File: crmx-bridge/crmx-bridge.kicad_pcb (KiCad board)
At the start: 4 copper layers, 100.5 x 76.8 mm, 94 parts, among them IC101 ESP32-S3-WROOM-1U-N4R2, J101 AFC07-S16FCC-00, J102 NC3FAAH2, J103 USB_C_Receptacle_USB2.0_16P, J104 NC3MAAH, J105 Conn_01x02_Pin, J106 AFC07-S16FCC-00, J201 Conn_01x04_Pin, Q101 DMP4025SFGQ-13, Q102 AO3400A, U101 TIMOTWO, U102 AP63200WU, U103 ISO3088DW, U104 SRV05-4, U105 ISO3088DW, U106 TEA1-0505, U107 TEA1-0505, U201 PEC12R-4215F-S0024

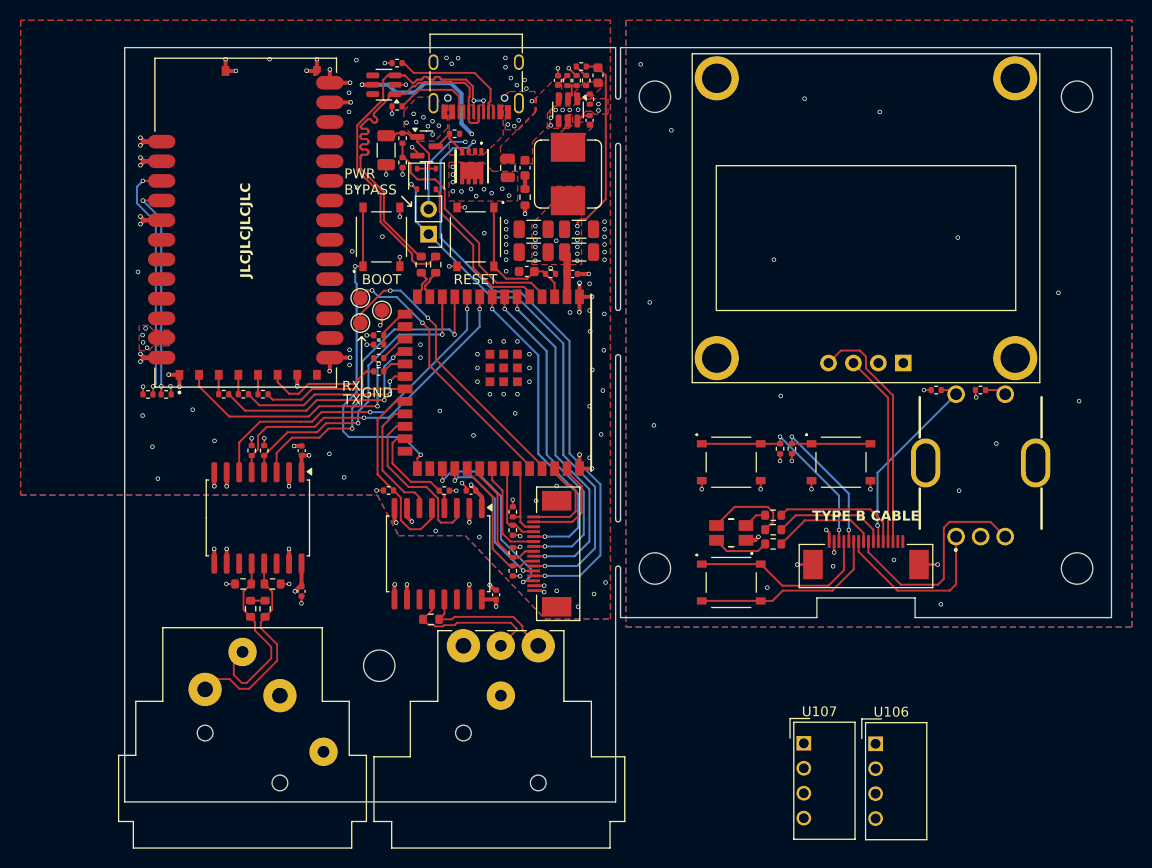
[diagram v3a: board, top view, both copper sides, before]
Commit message: smaller isolated supplies integrated, may re-arrange some more
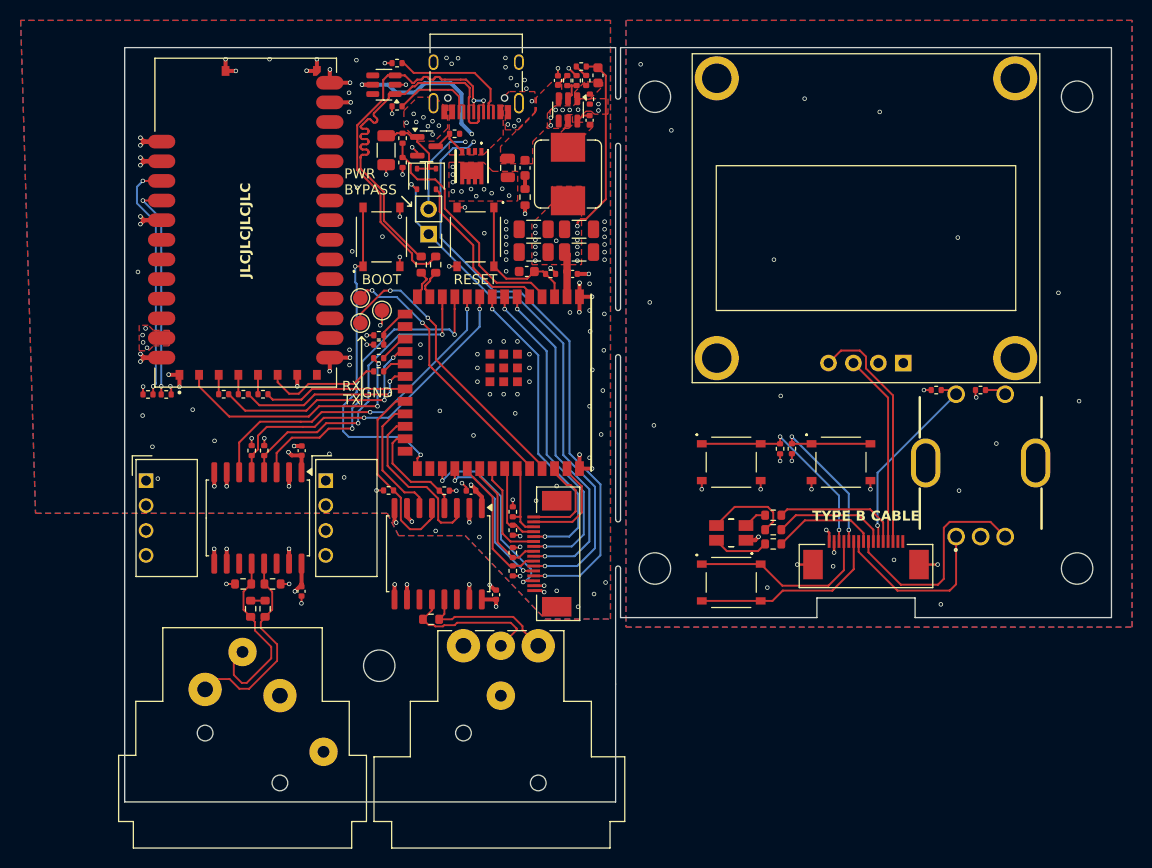
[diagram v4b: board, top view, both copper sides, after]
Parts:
- moved U107 72.1 mm to (119.5, 61.9)
- moved U106 62.1 mm to (137.8, 61.9)
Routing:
- net +3V3: track 37.7 -> 37.2 mm
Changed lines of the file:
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@@
 	(footprint "Converter_DCDC:Converter_DCDC_TRACO_TEA1-xxxx_THT"
 		(layer "F.Cu")
-		(at 186.4425 88.6075)
+		(at 119.45 61.85)
 		(descr "DCDC-Converter, TRACO, TEA1-xxxx, 1W, Rev. October 19. 2023 (Script generated with StandardBox.py) (https://www.tracopower.com/products/tea1.pdf)")
 		(tags "DCDC-Converter TRACO TEA1 THT SIP-4 1W")
@@
 			(at 1.6 -3.23 0)
 			(layer "F.SilkS")
+			(hide yes)
 			(effects
 				(font
@@
 	(footprint "Converter_DCDC:Converter_DCDC_TRACO_TEA1-xxxx_THT"
 		(layer "F.Cu")
-		(at 193.75 88.65)
+		(at 137.75 61.85)
 		(descr "DCDC-Converter, TRACO, TEA1-xxxx, 1W, Rev. October 19. 2023 (Script generated with StandardBox.py) (https://www.tracopower.com/products/tea1.pdf)")
 		(tags "DCDC-Converter TRACO TEA1 THT SIP-4 1W")
@@
 			(at 1.6 -3.23 0)
 			(layer "F.SilkS")
+			(hide yes)
 			(effects
 				(font
@@
 	)
 	(segment
+		(start 134.28 59.28)
+		(end 133.95 58.95)
+		(width 0.4064)
+		(layer "F.Cu")
+		(net 2)
+	)
+	(segment
+		(start 135.3 59.28)
+		(end 134.28 59.28)
+		(width 0.4064)
+		(layer "F.Cu")
+		(net 2)
+	)
+	(segment
 		(start 153.03 62.875)
 		(end 153.03 62.755)
@@
 	)
 	(segment
-		(start 135.285 59.295)
-		(end 135.3 59.28)
-		(width 0.4064)
-		(layer "F.Cu")
-		(net 2)
-	)
-	(segment
-		(start 136.045 59.28)
-		(end 136.05 59.275)
-		(width 0.4064)
-		(layer "F.Cu")
-		(net 2)
-	)
-	(segment
 		(start 156.8 71.55)
 		(end 157.525 71.55)
@@
 	)
 	(segment
-		(start 135.3 59.28)
-		(end 136.045 59.28)
-		(width 0.4064)
-		(layer "F.Cu")
-		(net 2)
-	)
-	(segment
 		(start 166.275 20.6)
 		(end 165.475 19.8)
@@
 	)
 	(via
-		(at 136.05 59.275)
-		(size 0.45)
-		(drill 0.3)
-		(layers "F.Cu" "B.Cu")
-		(net 2)
-	)
-	(via
 		(at 159.1 38.05)
 		(size 0.45)
@@
 	)
 	(via
+		(at 133.95 58.95)
+		(size 0.45)
+		(drill 0.3)
+		(layers "F.Cu" "B.Cu")
+		(net 2)
+	)
+	(via
 		(at 152.55 62.275)
 		(size 0.45)
@@
 	)
 	(segment
-		(start 136.05 59.275)
-		(end 136.05 60.525)
-		(width 0.4064)
-		(layer "In2.Cu")
-		(net 2)
-	)
-	(segment
 		(start 126.395 68.81)
 		(end 126.385 68.8)
@@
 		(polygon
 			(pts
-				(xy 143 63.325) (xy 145.175 67.45) (xy 151.961075 67.45) (xy 160.096321 75.95) (xy 166.75 75.95)
-				(xy 166.75 14.975) (xy 106.675 14.975) (xy 106.675 63.325)
+				(xy 144.017544 65.175) (xy 145.175 67.45) (xy 151.961075 67.45) (xy 160.096321 75.95) (xy 166.75 75.95)
+				(xy 166.75 14.975) (xy 106.675 14.975) (xy 108.19238 65.175)
 			)
 		)
@@
 		(polygon
 			(pts
-				(xy 166.797475 84.423806) (xy 151.904272 68.651888) (xy 144.364521 68.651888) (xy 142.5 64.925)
-				(xy 139.75 64.925) (xy 139.75 71.656336) (xy 141.752021 75.752797) (xy 141.752021 96.036888) (xy 166.777021 96.036888)
+				(xy 166.797475 84.423806) (xy 151.904272 68.651888) (xy 144.364521 68.651888) (xy 143.150376 66.225)
+				(xy 136.75 66.225) (xy 136.75 70.775621) (xy 141.752021 75.752797) (xy 141.752021 96.036888) (xy 166.777021 96.036888)
 			)
 		)
@@
 		(polygon
 			(pts
-				(xy 143 63.325) (xy 145.175 67.45) (xy 151.950717 67.45) (xy 160.090352 75.961826) (xy 166.75 75.966448)
-				(xy 166.75 16.875) (xy 115.075 16.875) (xy 115.075 63.325)
+				(xy 144.004824 65.15) (xy 145.175 67.45) (xy 151.950717 67.45) (xy 160.090352 75.961826) (xy 166.75 75.966448)
+				(xy 166.75 16.875) (xy 115.075 16.875) (xy 114.94856 65.15)
 			)
 		)
@@
 		(polygon
 			(pts
-				(xy 140.025 75.75) (xy 138.175 72) (xy 138.175 64.91) (xy 110.6 64.91) (xy 110.6 96.01) (xy 140.025 96.01)
+				(xy 140.025 75.75) (xy 135.75 71.639424) (xy 135.75 66.21) (xy 110.725 66.21) (xy 110.6 96.01) (xy 140.025 96.01)
 			)
 		)
@@
 		(polygon
 			(pts
-				(xy 166.795448 84.425033) (xy 151.901462 68.65) (xy 144.3625 68.65) (xy 142.5 64.925) (xy 139.75 64.925)
-				(xy 139.75 71.631725) (xy 141.75 75.72555) (xy 141.75 96.035) (xy 166.775 96.035)
+				(xy 166.795448 84.425033) (xy 151.901462 68.65) (xy 144.3625 68.65) (xy 143.15 66.225) (xy 136.8 66.225)
+				(xy 136.777251 70.802251) (xy 141.75 75.72555) (xy 141.75 96.035) (xy 166.775 96.035)
 			)
 		)
@@
 		(polygon
 			(pts
-				(xy 149.525 28.95) (xy 158.1 28.8) (xy 158.1 44.575) (xy 142.925 59.75) (xy 121.625 59.75) (xy 121.625 56.275)
-				(xy 124.35 53.55) (xy 136.825 53.55) (xy 149.525 40.85)
+				(xy 149.525 28.95) (xy 158.1 28.8) (xy 158.1 44.575) (xy 138.725 65.125) (xy 118.325 65.125) (xy 118.325 59.6)
+				(xy 134.55 59.6) (xy 149.525 44.625)
 			)
 		)
@@
 		(polygon
 			(pts
-				(xy 140.025 75.75) (xy 138.175 72) (xy 138.175 64.91) (xy 107.7 64.91) (xy 107.7 100.235) (xy 140.025 99.975)
+				(xy 140.025 75.75) (xy 135.75 71.644867) (xy 135.75 66.21) (xy 107.825 66.21) (xy 107.7 100.235)
+				(xy 140.025 99.975)
 			)
 		)
@@
 		(polygon
 			(pts
-				(xy 143 63.325) (xy 145.175 67.45) (xy 151.983187 67.45) (xy 160.100769 75.95) (xy 166.75 75.95)
-				(xy 166.75 14.975) (xy 108.675 14.975) (xy 108.675 63.325)
+				(xy 144.004824 65.15) (xy 145.175 67.45) (xy 151.983187 67.45) (xy 160.100769 75.95) (xy 166.75 75.95)
+				(xy 166.75 14.975) (xy 108.675 14.975) (xy 108.599169 65.15)
 			)
 		)

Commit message: Rev to v0.2
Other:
- board text added: "DMX IO Device HMI V0.2 Chris Markus, 2024"
- board text added: "DMX IO Device V0.2 Chris Markus, 2024"
- board text removed: "DMX IO Device HMI V0.1 Chris Markus, 2024"
- board text removed: "DMX IO Device V0.1 Chris Markus, 2024"
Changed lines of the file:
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@@
 		(layer "Edge.Cuts")
 	)
-	(gr_text "DMX IO Device HMI V0.1\nChris Markus, 2024"
+	(gr_text "DMX IO Device HMI V0.2\nChris Markus, 2024"
 		(at 192.775 37.8 0)
 		(layer "B.SilkS")
@@
 		)
 	)
-	(gr_text "DMX IO Device V0.1\nChris Markus, 2024"
+	(gr_text "DMX IO Device V0.2\nChris Markus, 2024"
 		(at 142.275 47.575 0)
 		(layer "B.SilkS")

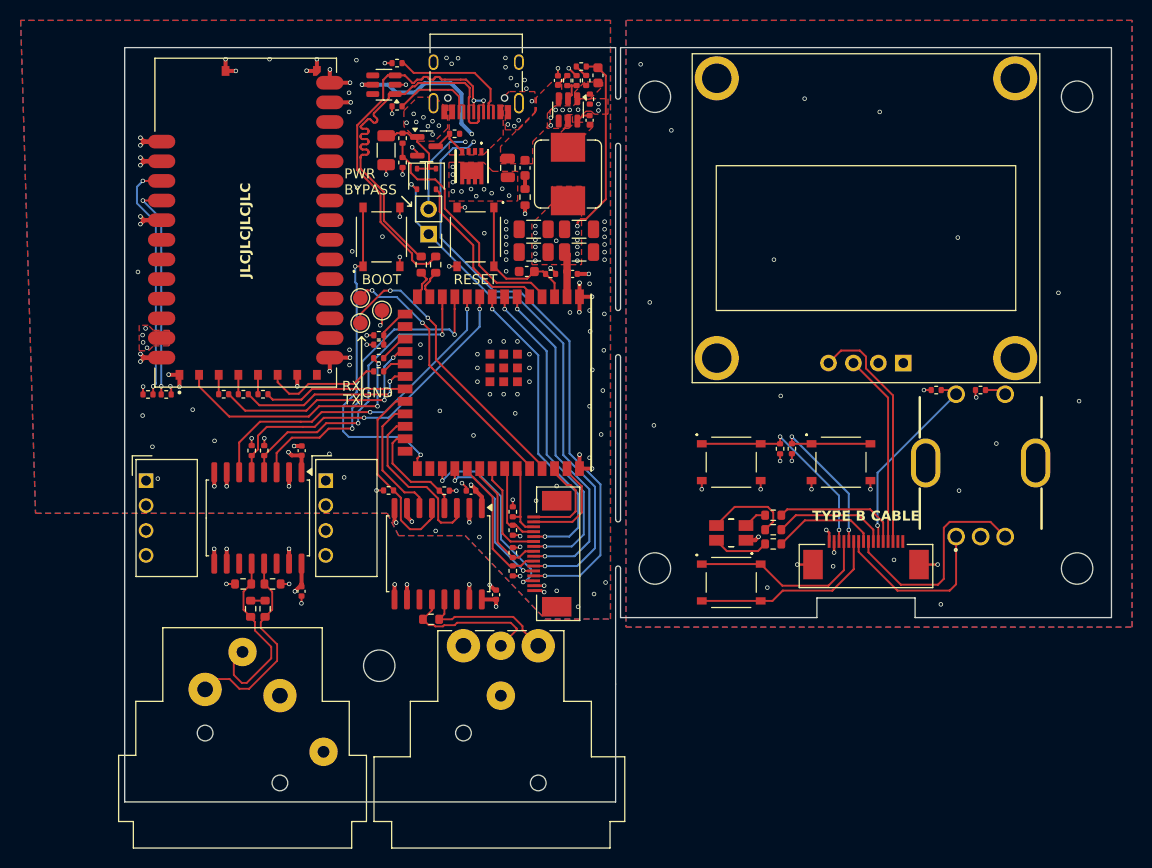
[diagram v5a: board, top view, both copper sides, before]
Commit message: Finished layout with smaller power converters
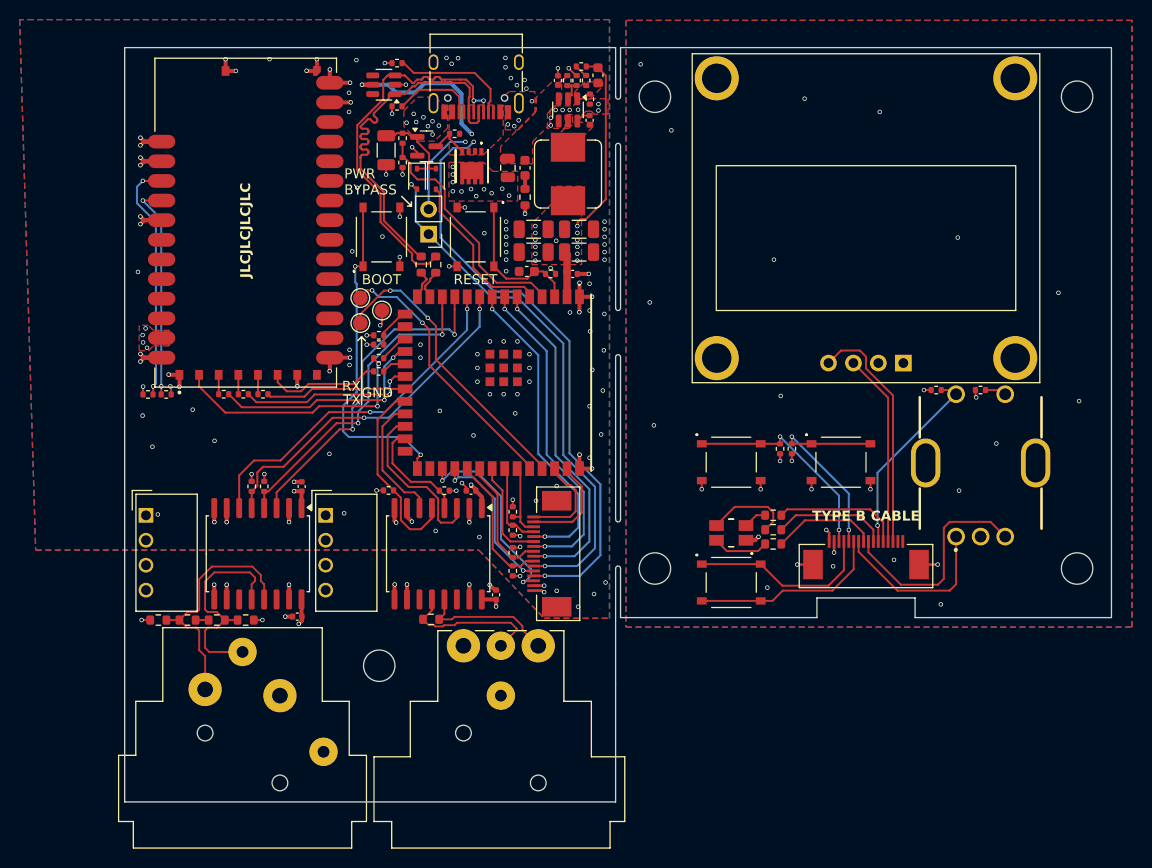
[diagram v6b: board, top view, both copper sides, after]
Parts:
- moved R105 12.2 mm to (120.7, 76.0), turned to 180 degrees
- moved R125 7.98 mm to (123.7, 76.0), turned to 180 degrees
- moved R104 3.68 mm to (129.6, 76.0), turned to 180 degrees
- moved C101 3.65 mm to (135.3, 62.5)
- moved R121 3.65 mm to (130.2, 62.4)
- moved R122 3.65 mm to (131.5, 62.4)
- moved U103 3.65 mm to (130.8, 69.3)
- moved R103 3.64 mm to (126.7, 76.0), turned to 180 degrees
- moved U106 3.53 mm to (137.7, 65.4)
- moved U107 3.53 mm to (119.4, 65.4)
- moved C102 2.61 mm to (134.8, 75.7), turned to 180 degrees
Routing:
- net /DMX_OUT_N: track 20.7 -> 25.4 mm
- net /DMX_OUT_P: track 19.0 -> 22.8 mm
- net /DMX_OUT_TX: track 34.4 -> 36.1 mm
- net /DMX_OUT_NRE: track 31.6 -> 33.1 mm
- net /DMX_OUT_DE: track 34.2 -> 35.7 mm
- net /DMX_OUT_RX: track 32.8 -> 34.2 mm
- net +3V3: track 37.2 -> 36.5 mm

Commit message: Split up PCBs into separate files, Ordered V0.3
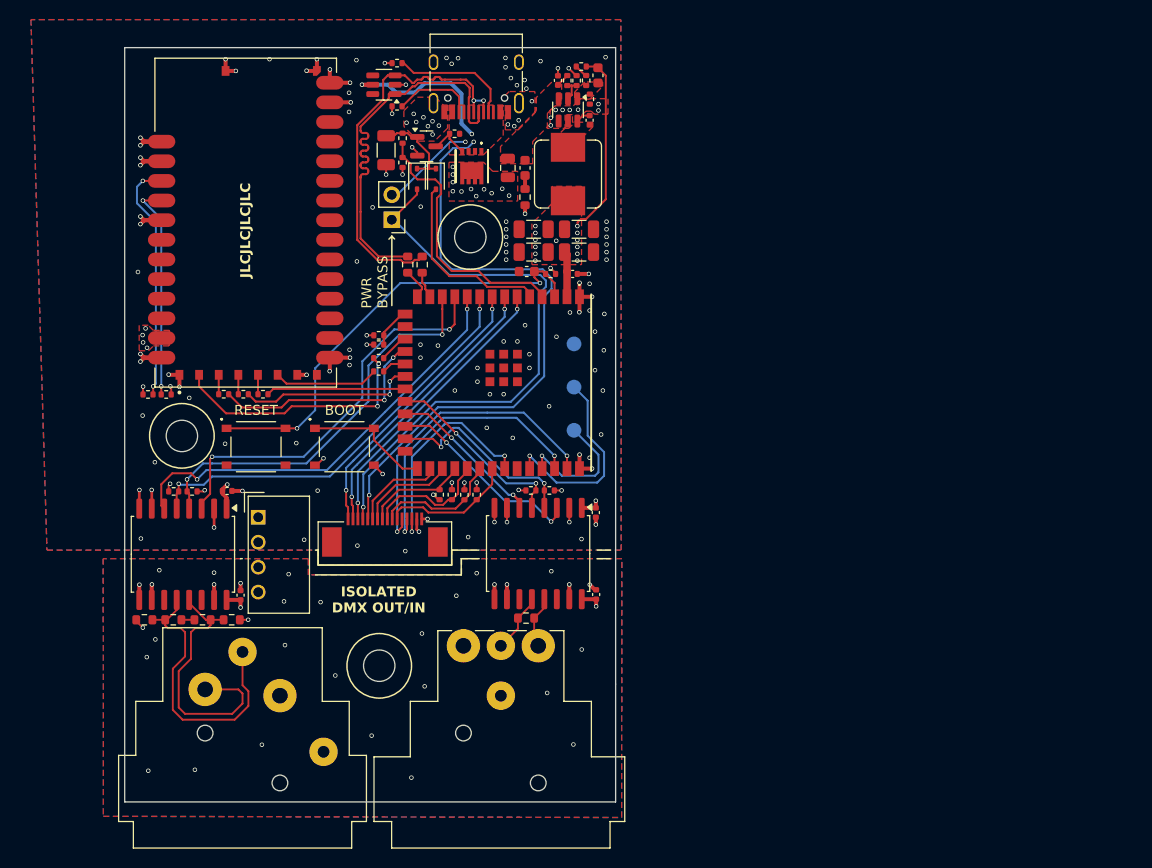
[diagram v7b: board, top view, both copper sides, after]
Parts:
- removed D201: ASMB-MTB0-0A3A2, ASMB-MTB0-0A3A2:ASMBMTB00A3A2
- removed H104, H105: MountingHole, MountingHole:MountingHole_3.2mm_M3
- removed J101: AFC07-S16FCC-00, AFC07-S16FCC-00:AFC07S16FCC00
- removed J201: Conn_01x04_Pin, Oled:OLED_1.3
- removed R205, R207, R208: 10k, Resistor_SMD:R_0402_1005Metric
- removed R206: 0R, Resistor_SMD:R_0402_1005Metric
- removed R209, R210, R211: 150, Resistor_SMD:R_0603_1608Metric
- removed S201, S202, S203: TS-1187A-B-A-B, LIB_TS-1187A-B-A-B:TS1187ABAB
- removed U107: TEA1-0505, Converter_DCDC:Converter_DCDC_TRACO_TEA1-xxxx_THT
- removed U201: PEC12R-4215F-S0024, PEC12R:PEC12R-4XXXF-SXXXX
- TP101, TP102, TP103: moved to B.Cu
- moved H103 97.5 mm to (123.1, 57.3)
- moved H102 70.4 mm to (152.5, 37.0)
- moved S101 30.9 mm to (130.7, 58.4), turned to 0 degrees
- moved TP102 24.4 mm to (163.0, 56.7), turned to 0 degrees
- moved TP101 23.6 mm to (163.0, 52.3), turned to 0 degrees
- moved S102 21.7 mm to (139.7, 58.4), turned to 0 degrees
- moved TP103 19.9 mm to (163.0, 47.9), turned to 180 degrees
- moved J106 17.5 mm to (143.8, 68.1), turned to 0 degrees
- moved R126 14.5 mm to (158.6, 62.9)
- moved C113 12.9 mm to (165.3, 65.1), turned to -90 degrees
- moved R113 10.8 mm to (149.3, 63.3)
- moved R127 10.7 mm to (160.5, 62.9)
- moved R104 10.3 mm to (119.3, 76.0), turned to 0 degrees
- moved C114 10.2 mm to (165.3, 73.5)
- moved U105 10.2 mm to (159.4, 69.3)
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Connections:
- C102 pad 1: /VCC_ISO_2 -> /VCC_ISO
- C102 pad 2: /GND_ISO_2 -> GNDS
- C114 pad 1: /VCC_ISO_1 -> /VCC_ISO
- C114 pad 2: /GND_ISO_1 -> GNDS
- IC101 pad 28: unconnected-(IC101-IO35-Pad28) -> /OK_BTN
- IC101 pad 29: /OK_BTN -> /BK_BTN
- IC101 pad 30: /BK_BTN -> /ENC1.A
- IC101 pad 31: /ENC1.A -> /ENC1.B
- IC101 pad 32: /ENC1.B -> /OLED_SCL
- IC101 pad 33: /ENC1.SW -> /OLED_SDA
- IC101 pad 34: /OLED_SCL -> /ENC1.SW
- IC101 pad 35: /OLED_SDA -> unconnected-(IC101-IO42-Pad35)
- J102 pad 1: /GND_ISO_2 -> GNDS
- J102 pad G: /GND_ISO_2 -> GNDS
- J104 pad 1: /GND_ISO_1 -> GNDS
- J104 pad G: /GND_ISO_1 -> GNDS
- J106 pad 1: GND -> /LED_R
- J106 pad 10: /LED_G -> /OLED_SCL
- J106 pad 11: /ENC1.SW -> /OLED_SDA
- J106 pad 12: /LED_R -> /IO1
- J106 pad 13: /OLED_SCL -> /IO2
- J106 pad 14: /OLED_SDA -> /ENC1.SW
- J106 pad 15: /IO1 -> GND
- J106 pad 16: /IO2 -> +3V3
- J106 pad 2: +3V3 -> /LED_G
- J106 pad 3: /OK_BTN -> /LED_B
- J106 pad 4: /VUSB_IN -> /PWR_BTN_LO
- J106 pad 5: /BK_BTN -> /VUSB_IN
- J106 pad 6: /PWR_BTN_LO -> /OK_BTN
- J106 pad 7: /ENC1.A -> /BK_BTN
- J106 pad 8: /LED_B -> /ENC1.A
- R104 pad 1: /VCC_ISO_2 -> /VCC_ISO
- R105 pad 2: /GND_ISO_2 -> GNDS
- U103 pad 10: /GND_ISO_2 -> GNDS
- U103 pad 15: /GND_ISO_2 -> GNDS
- U103 pad 16: /VCC_ISO_2 -> /VCC_ISO
- U103 pad 9: /GND_ISO_2 -> GNDS
- U105 pad 10: /GND_ISO_1 -> GNDS
- U105 pad 15: /GND_ISO_1 -> GNDS
- U105 pad 16: /VCC_ISO_1 -> /VCC_ISO
- U105 pad 9: /GND_ISO_1 -> GNDS
- U106 pad 3: /GND_ISO_1 -> GNDS
- U106 pad 4: /VCC_ISO_1 -> /VCC_ISO
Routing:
- net /VUSB: track 0.00 -> 44.9 mm
- net /EN: track 14.9 -> 45.9 mm, vias 0 -> 2
- net /HMI/OLED_SDA: track 24.6 -> 0.00 mm
- net /HMI/ENC_B: track 22.7 -> 0.00 mm
- net /HMI/OK_BTN: track 21.9 -> 0.00 mm, vias 2 -> 0
- net /HMI/BK_BTN: track 21.8 -> 0.00 mm, vias 2 -> 0
- net /IO1: track 10.4 -> 31.7 mm, vias 0 -> 2
- net /IO0: track 34.7 -> 13.4 mm, vias 2 -> 0
- net /HMI/ENC_SW: track 20.0 -> 0.00 mm, vias 1 -> 0
- net /HMI/OLED_SCL: track 19.6 -> 0.00 mm
- net /HMI/PWR_BTN_LO: track 19.6 -> 0.00 mm
- net /HMI/PWR_BTN_HI: track 19.0 -> 0.00 mm
- net /IO2: track 9.99 -> 28.9 mm, vias 0 -> 2
- net /HMI/ENC_A: track 17.7 -> 0.00 mm
- net /TXD0: track 30.1 -> 13.3 mm, vias 2 -> 1
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- added copper zone on In2.Cu, net /VCC_ISO
- added copper zone on B.Cu, net GNDS
- added copper zone on F.Cu, net GNDS
- added copper zone on In1.Cu, net GNDS
- removed copper zone on In1.Cu, net /GND_ISO_1
- removed copper zone on In1.Cu, net /GND_ISO_2
- removed copper zone on In2.Cu, net /HMI/3V3
- removed copper zone on In2.Cu, net /VCC_ISO_1
- removed copper zone on In2.Cu, net /VCC_ISO_2
- removed copper zone on B.Cu, net GND1
- removed copper zone on F.Cu, net GND1
- removed copper zone on In1.Cu, net GND1
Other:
- board size 100.5 x 76.8 mm -> 50 x 76.8 mm
- board text added: "DMX IO Device V0.3 Chris Markus, 2024"
- board text added: "ISOLATED DMX OUT/IN"
- board text removed: "DMX IO Device HMI V0.2 Chris Markus, 2024"
- board text removed: "DMX IO Device V0.2 Chris Markus, 2024"
- board text removed: "TYPE B CABLE"
